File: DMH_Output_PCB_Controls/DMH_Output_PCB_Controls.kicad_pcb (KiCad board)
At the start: 2 copper layers, 48 x 121 mm, 90 parts, among them J10 Conn_01x06, J11 Conn_01x06, J12 Conn_01x06, J13 Conn_01x06, J21 Conn_01x02, J22 Conn_01x02, Q1 BC558, Q2 BC558, U2 LM339, U21 LM4040LP-10, U24 LM339, U25 LM339, U3 LM339, U4 LM339, U5 LM339, U6 LM339

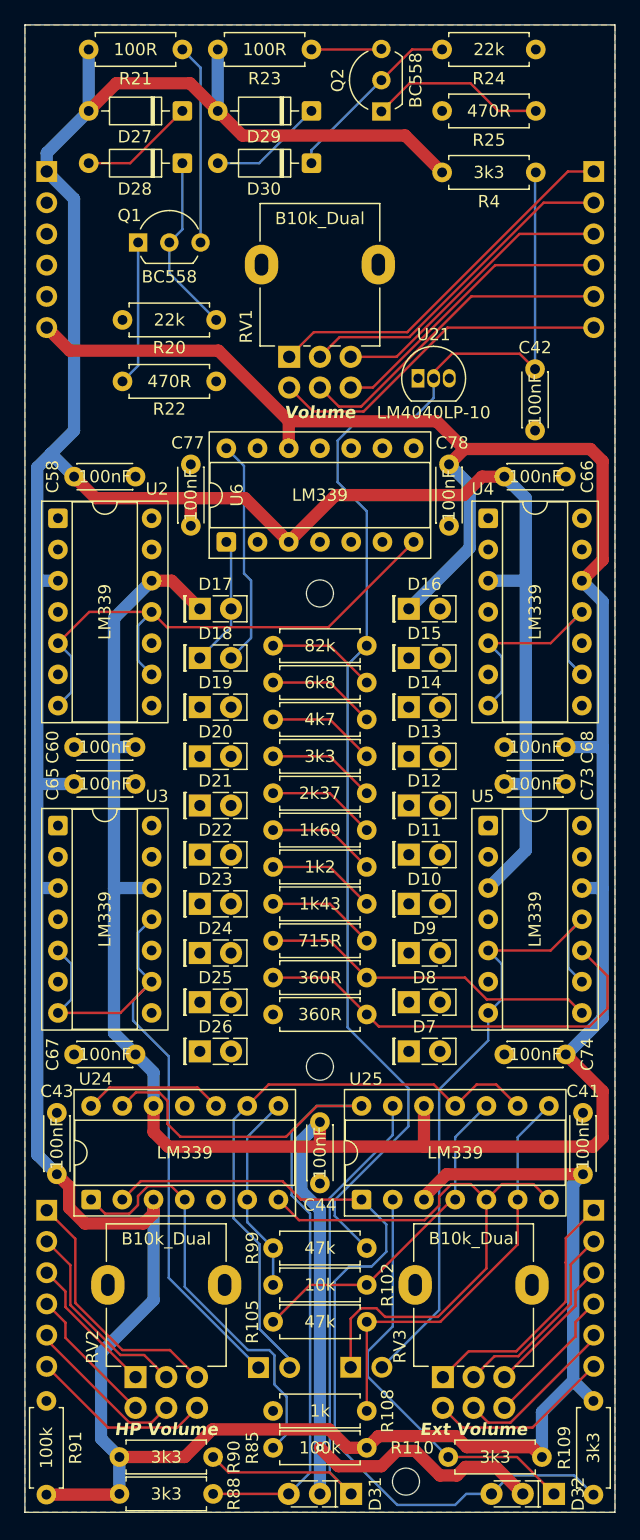
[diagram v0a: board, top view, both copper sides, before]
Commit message: Controls PCB routing in progress
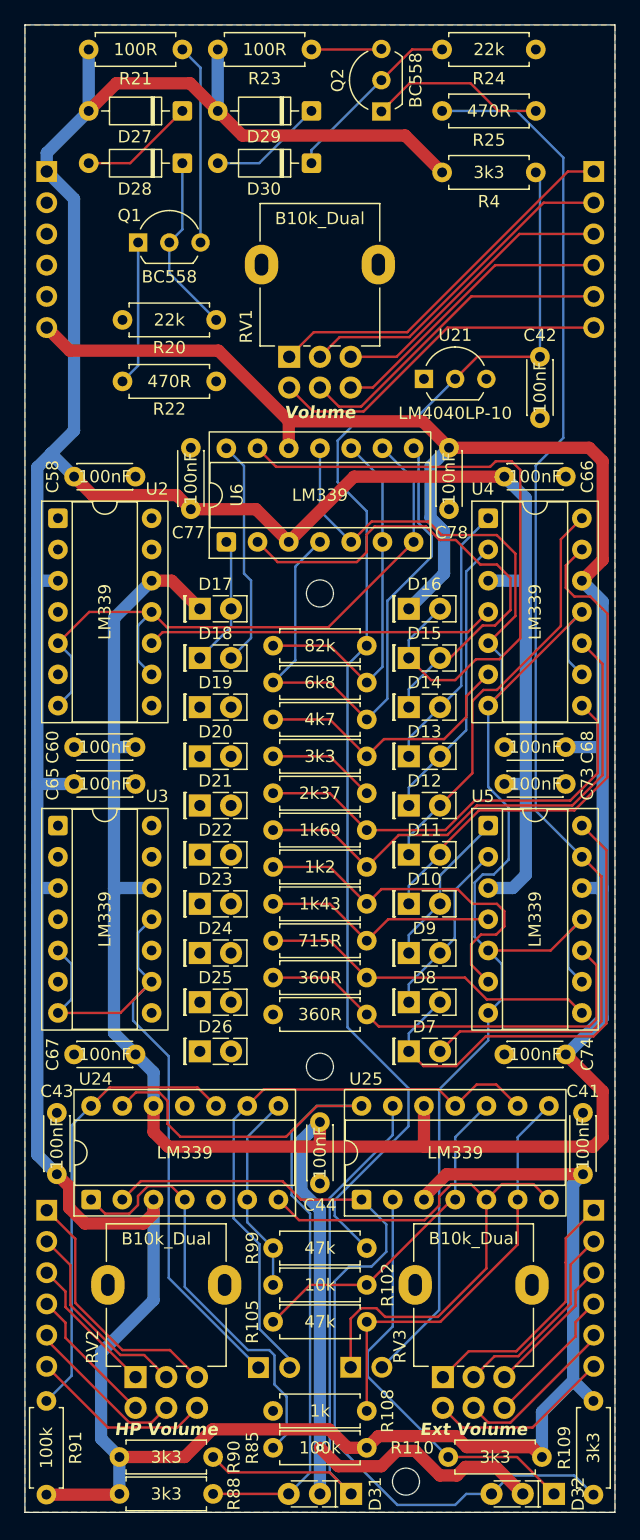
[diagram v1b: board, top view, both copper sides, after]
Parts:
- J11, J12: value Conn_01x06 -> Conn_01x06_PinHeader
- U21: footprint Package_TO_SOT_THT:TO-92_Inline -> Package_TO_SOT_THT:TO-92L_Inline_Wide
- moved C77 1.35 mm to (64.5, 81.9)
- moved C78 1.35 mm to (85.5, 81.9)
- moved C42 1.08 mm to (92.9, 69.5)
- moved U21 0.48 mm to (83.5, 71.3)
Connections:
- net /Balanced Line Driver/L_Ch_OUT renamed Net-(J11A-Pin_1)
- net /Balanced Line Driver/R_Ch_OUT renamed Net-(J11F-Pin_6)
- net /PreAmp/RV3A_p1 renamed /PreAmp/RV3A_p1_C
- net /PreAmp/RV3A_p2 renamed /PreAmp/RV3A_p2_C
- net /PreAmp/RV3A_p3 renamed /PreAmp/RV3A_p3_C
- net /PreAmp/RV3B_p4 renamed /PreAmp/RV3B_p4_C
- net /PreAmp/RV3B_p5 renamed /PreAmp/RV3B_p5_C
- net /PreAmp/RV3B_p6 renamed /PreAmp/RV3B_p6_C
- net Input_Meter_L renamed Input_Meter_L_C
- net Input_Meter_R renamed Input_Meter_R_C
- net Output_Meter_L renamed Output_Meter_L_C
- net Output_Meter_R renamed Output_Meter_R_C
- J11 pad 3: /Gain Trimmer/L_Gain_IN -> Net-(J11C-Pin_3)
- J11 pad 4: /Gain Trimmer/R_Gain_IN -> Net-(J11D-Pin_4)
- J12 pad 1: /Gain Trimmer/L_Gain_IN -> Net-(J12A-Pin_1)
- J12 pad 6: /Gain Trimmer/R_Gain_IN -> Net-(J12F-Pin_6)
- RV1 pad 3: /Gain Trimmer/L_Gain_IN -> Net-(J11C-Pin_3)
- RV1 pad 6: /Gain Trimmer/R_Gain_IN -> Net-(J11D-Pin_4)
- RV2 pad 3: /Gain Trimmer/L_Gain_IN -> Net-(J12A-Pin_1)
- RV2 pad 6: /Gain Trimmer/R_Gain_IN -> Net-(J12F-Pin_6)
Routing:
- net Net-(D7-A): track 0.00 -> 99.0 mm
- net Output_Meter_R_C: track 73.7 -> 130.6 mm
- net Net-(D15-K): track 0.00 -> 52.5 mm
- net /Gain Trimmer/L_Gain_IN: track 44.8 -> 0.00 mm
- net Net-(D10-K): track 0.00 -> 42.8 mm
- net Net-(D14-K): track 0.00 -> 40.0 mm
- net Net-(D7-K): track 0.00 -> 40.0 mm
- net /Gain Trimmer/R_Gain_IN: track 38.8 -> 0.00 mm
- net Net-(U6A--): track 8.86 -> 46.7 mm
- net Net-(D11-K): track 0.00 -> 33.8 mm
- net Net-(U2A--): track 8.86 -> 42.6 mm
- net Net-(U2C--): track 8.86 -> 37.3 mm
- net Net-(U2B--): track 8.86 -> 35.6 mm
- net Net-(U24C--): track 11.4 -> 36.9 mm
- net Net-(J11C-Pin_3): track 0.00 -> 23.9 mm
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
